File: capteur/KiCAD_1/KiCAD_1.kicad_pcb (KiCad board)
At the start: 2 copper layers, 68.6 x 59.1 mm, 25 parts, among them J1 Power, J2 Digital/PWM, J3 Analog, J4 Digital/PWM, U1 Bluetooth_HC05, U2 LTC1050CN8, U3 DM_OLED_096_636, U4 Graphite_sensor, U5 Rotary_encoder_KY_040, U6 Potentionmettre_MCP41010, U7 Flex_sensor, U8 Servomotor

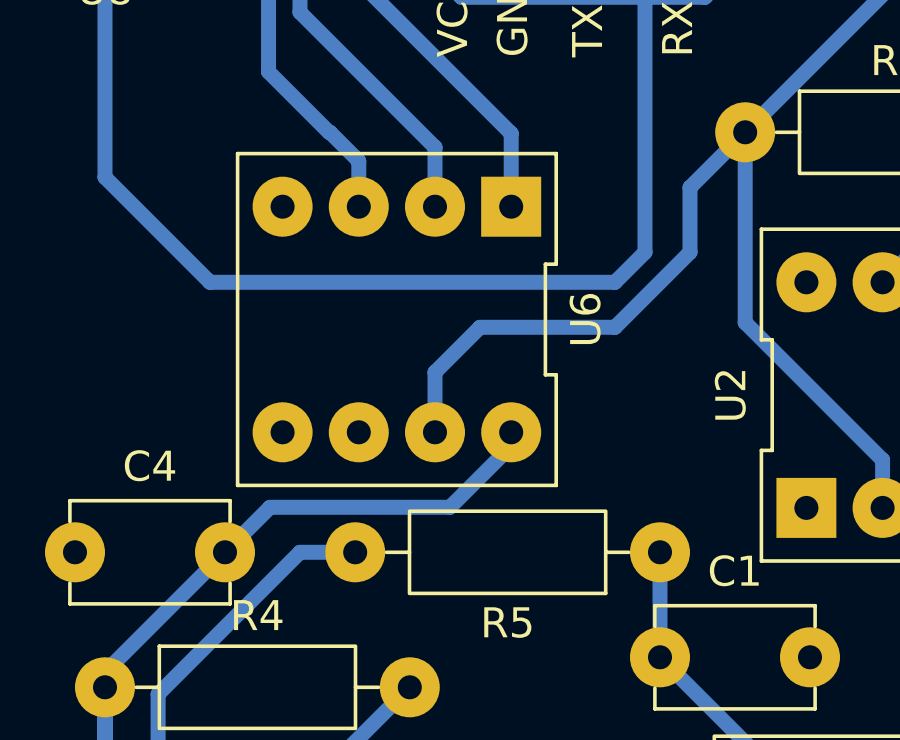
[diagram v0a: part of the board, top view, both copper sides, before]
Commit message: VCC track now correctly connected
Changes to make; VCC to 5V+

VCC now connected from potentiometer to VCC track; from R3 to
Servomoteur_VCC
Potentiomettre_GND is CORRECTLY connected to the ground plane, it's
kinda hard to see at first look, but closer inspection makes it obvious
VCC now connects to C4, R4 and U4
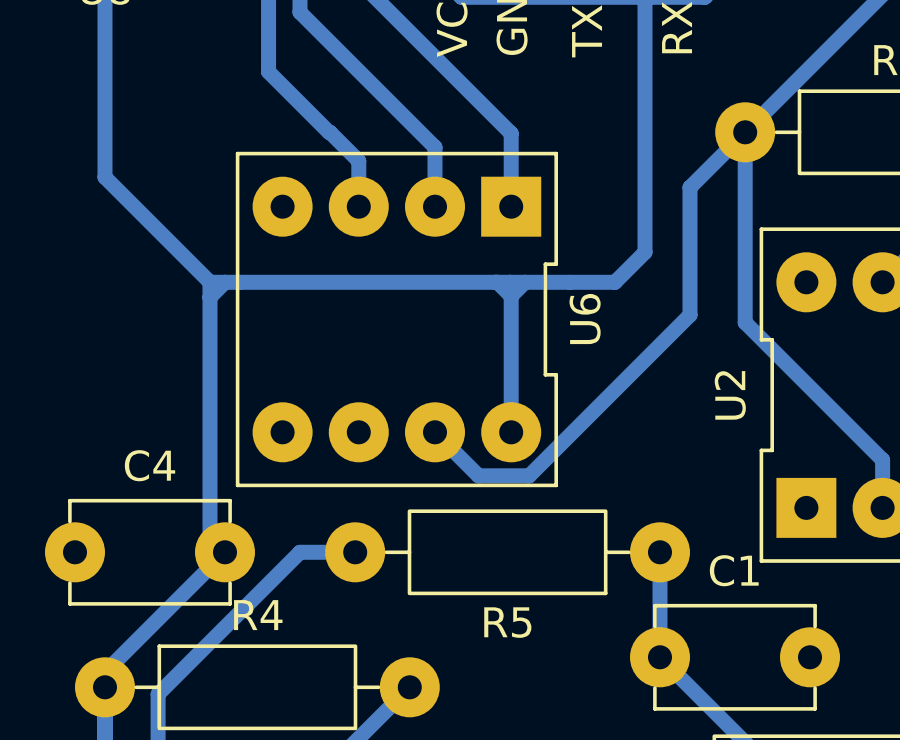
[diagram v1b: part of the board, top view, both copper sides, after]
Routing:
- net VCC: track 196.1 -> 200.9 mm
- net Pot_1: track 41.3 -> 42.5 mm
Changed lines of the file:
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@@
+	)
+	(segment
+		(start 135 70)
+		(end 133.5 70)
+		(width 0.5)
+		(layer "B.Cu")
+		(net 22)
 	)
 	(segment
@@
 	)
 	(segment
+		(start 133.04 75)
+		(end 133.04 70.46)
+		(width 0.5)
+		(layer "B.Cu")
+		(net 22)
+	)
+	(segment
 		(start 123.5 79)
 		(end 119.5 83)
@@
 	)
 	(segment
+		(start 133.04 70.04)
+		(end 133 70)
+		(width 0.5)
+		(layer "B.Cu")
+		(net 22)
+	)
+	(segment
 		(start 157.779 76)
 		(end 157.779 82.721)
@@
 	)
 	(segment
+		(start 132.58 70)
+		(end 133.04 70.46)
+		(width 0.5)
+		(layer "B.Cu")
+		(net 22)
+	)
+	(segment
+		(start 123.5 70)
+		(end 123 70)
+		(width 0.5)
+		(layer "B.Cu")
+		(net 22)
+	)
+	(segment
 		(start 137.5 60.5)
 		(end 137.5 69)
@@
 	)
 	(segment
+		(start 133 70)
+		(end 132.5 70)
+		(width 0.5)
+		(layer "B.Cu")
+		(net 22)
+	)
+	(segment
+		(start 123 70)
+		(end 123 70.5)
+		(width 0.5)
+		(layer "B.Cu")
+		(net 22)
+	)
+	(segment
 		(start 159.5 66.5)
 		(end 159.5 67)
@@
 	)
 	(segment
-		(start 123.5 79)
-		(end 125 77.5)
-		(width 0.5)
-		(layer "B.Cu")
-		(net 22)
-	)
-	(segment
 		(start 115.062 55)
 		(end 107.5 62.562)
@@
 	)
 	(segment
+		(start 124 70)
+		(end 123.5 70)
+		(width 0.5)
+		(layer "B.Cu")
+		(net 22)
+	)
+	(segment
+		(start 123 70.5)
+		(end 123 78.5)
+		(width 0.5)
+		(layer "B.Cu")
+		(net 22)
+	)
+	(segment
 		(start 158 66.5)
 		(end 159.5 66.5)
@@
 	)
 	(segment
-		(start 131 77.5)
-		(end 133.04 75.46)
+		(start 132.5 70)
+		(end 124 70)
 		(width 0.5)
 		(layer "B.Cu")
@@
 	)
 	(segment
+		(start 123 70.5)
+		(end 123.5 70)
+		(width 0.5)
+		(layer "B.Cu")
+		(net 22)
+	)
+	(segment
 		(start 107.5 62.562)
 		(end 107.5 75.5)
@@
 	)
 	(segment
-		(start 125 77.5)
-		(end 131 77.5)
-		(width 0.5)
-		(layer "B.Cu")
-		(net 22)
-	)
-	(segment
 		(start 162 67.684)
 		(end 162 71.779)
@@
 	)
 	(segment
+		(start 123 78.5)
+		(end 123.5 79)
+		(width 0.5)
+		(layer "B.Cu")
+		(net 22)
+	)
+	(segment
 		(start 154.5 87)
 		(end 154.5 86)
@@
 	)
 	(segment
+		(start 132.5 70)
+		(end 132.58 70)
+		(width 0.5)
+		(layer "B.Cu")
+		(net 22)
+	)
+	(segment
 		(start 146 97.5)
 		(end 150 93.5)
@@
 	)
 	(segment
+		(start 133.04 70.46)
+		(end 133.5 70)
+		(width 0.5)
+		(layer "B.Cu")
+		(net 22)
+	)
+	(segment
 		(start 150 91.5)
 		(end 154.5 87)
@@
 	(segment
 		(start 136.5 70)
-		(end 123 70)
+		(end 135 70)
 		(width 0.5)
 		(layer "B.Cu")
@@
 	)
 	(segment
+		(start 133.5 70)
+		(end 133 70)
+		(width 0.5)
+		(layer "B.Cu")
+		(net 22)
+	)
+	(segment
 		(start 157.779 82.721)
 		(end 154.5 86)
@@
 	)
 	(segment
-		(start 132 71.5)
-		(end 136.5 71.5)
-		(width 0.5)
-		(layer "B.Cu")
-		(net 33)
-	)
-	(segment
-		(start 139 69)
-		(end 139 66.84)
+		(start 131.951 76.451)
+		(end 133.641024 76.451)
 		(width 0.5)
 		(layer "B.Cu")
@@
 	)
 	(segment
-		(start 130.5 75)
-		(end 130.5 73)
+		(start 133.641024 76.451)
+		(end 139 71.092024)
 		(width 0.5)
 		(layer "B.Cu")
@@
 	)
 	(segment
+		(start 145.5 60.34)
+		(end 145.5 57)
+		(width 0.5)
+		(layer "B.Cu")
+		(net 33)
+	)
+	(segment
+		(start 140.84 71.3433)
+		(end 145.42 75.9233)
+		(width 0.5)
+		(layer "B.Cu")
+		(net 33)
+	)
+	(segment
+		(start 130.5 75)
+		(end 131.951 76.451)
+		(width 0.5)
+		(layer "B.Cu")
+		(net 33)
+	)
+	(segment
+		(start 139 71.092024)
+		(end 139 66.84)
+		(width 0.5)
+		(layer "B.Cu")
+		(net 33)
+	)
+	(segment
+		(start 145.42 77.52)
+		(end 145.42 75.9233)
+		(width 0.5)
+		(layer "B.Cu")
+		(net 33)
+	)
+	(segment
 		(start 139 66.84)
 		(end 140.84 65)
 		(width 0.5)
 		(layer "B.Cu")
-		(net 33)
-	)
-	(segment
-		(start 136.5 71.5)
-		(end 139 69)
-		(width 0.5)
-		(layer "B.Cu")
-		(net 33)
-	)
-	(segment
-		(start 145.5 60.34)
-		(end 145.5 57)
-		(width 0.5)
-		(layer "B.Cu")
-		(net 33)
-	)
-	(segment
-		(start 140.84 71.3433)
-		(end 145.42 75.9233)
-		(width 0.5)
-		(layer "B.Cu")
-		(net 33)
-	)
-	(segment
-		(start 145.42 77.52)
-		(end 145.42 75.9233)
-		(width 0.5)
-		(layer "B.Cu")
-		(net 33)
-	)
-	(segment
-		(start 130.5 73)
-		(end 132 71.5)
-		(width 0.5)
-		(layer "B.Cu")

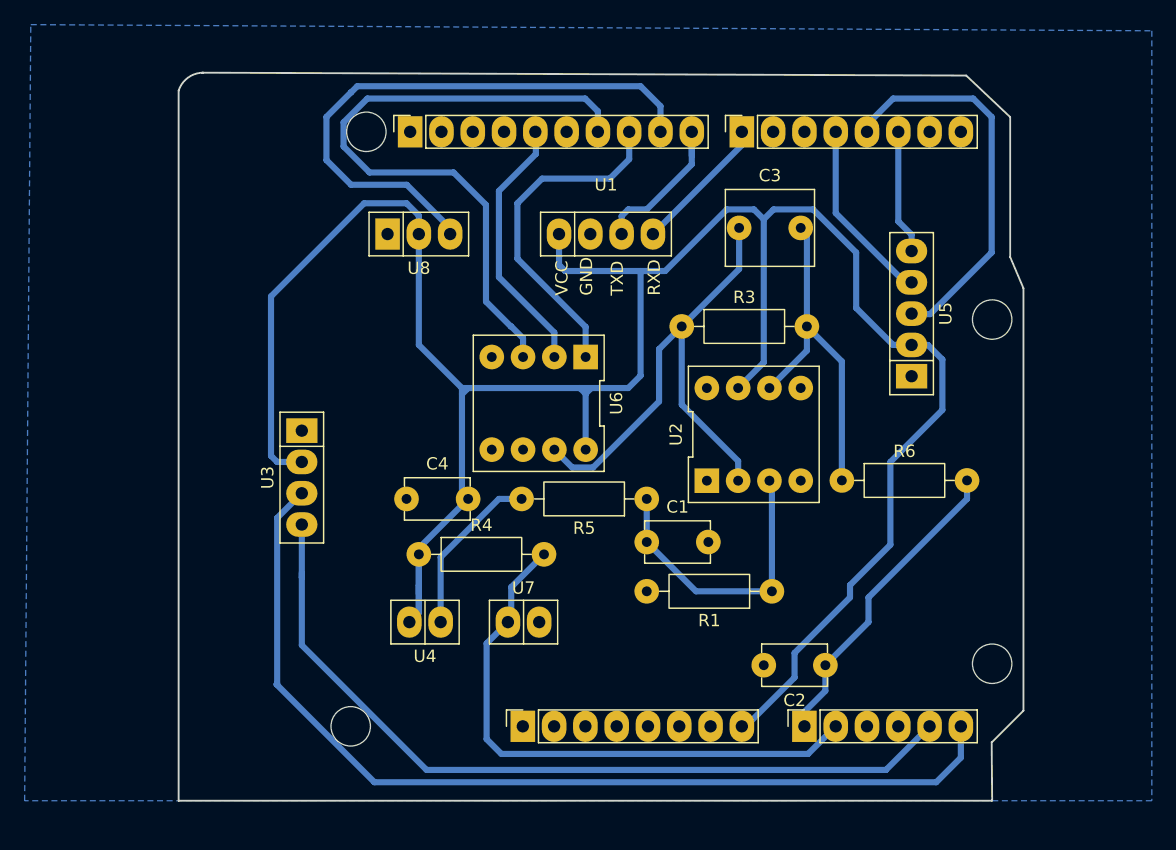
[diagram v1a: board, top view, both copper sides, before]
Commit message: PCB updated with VCC to +5V, GND plane connected
Flex and servomoteur empreintes updated, with the pin numbers
+5V track moved for spacing
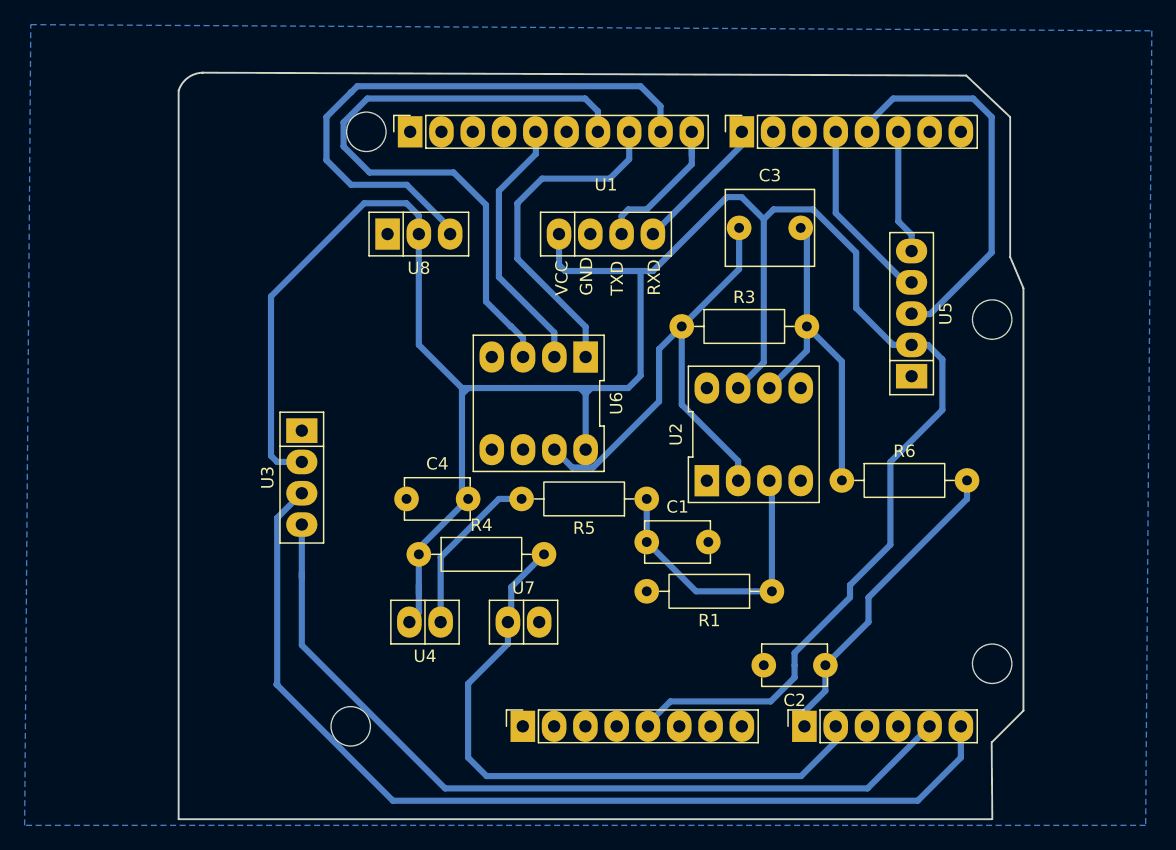
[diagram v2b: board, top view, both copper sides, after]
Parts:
- U1: footprint graphite_empreinte:Bluetooth_HC05 -> empreinte_library:Bluetooth_HC05_header
- U2: footprint graphite_empreinte:LTC1050_1 -> empreinte_library:LTC1050_header
- U3: value DM_OLED_096_636 -> DM-OLED096-636; footprint graphite_empreinte:OLED_header -> empreinte_library:OLED_header
- U4, U7: footprint graphite_empreinte:2_pin_header -> empreinte_library:2_pin_header
- U5: footprint graphite_empreinte:Rotatory_encoder_header -> empreinte_library:Rotary_encoder_header
- U6: value Potentionmettre_MCP41010 -> Potentionmeter_MCP41010; footprint graphite_empreinte:LTC1050_1 -> empreinte_library:Potentionmeter_header
- U8: value Servomotor -> Servo_motor; footprint graphite_empreinte:Servomotor_header -> empreinte_library:Servomotor_header
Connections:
- C4 pad 2: VCC -> +5V
- J1 pad 8: VCC -> /Vin
- R4 pad 1: VCC -> +5V
- U1 pad 1: VCC -> +5V
- U2 pad 7: VCC -> +5V
- U3 pad 2: VCC -> +5V
- U4 pad 1: VCC -> +5V
- U5 pad 2: VCC -> +5V
- U6 pad 8: VCC -> +5V
- U8 pad 2: VCC -> +5V
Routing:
- net +5V: track 0.00 -> 204.7 mm
- net VCC: track 200.9 -> 0.00 mm
- net Flex_output: track 46.7 -> 51.9 mm
- net SCL: track 78.6 -> 79.8 mm
- net SDA: track 66.8 -> 68.0 mm
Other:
- board size 68.6 x 59.1 mm -> 68.6 x 60.6 mm
